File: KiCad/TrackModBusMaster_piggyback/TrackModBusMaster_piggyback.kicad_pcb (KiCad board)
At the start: 2 copper layers, 40 x 77 mm, 66 parts, among them J1 Conn_02x08_Top_Bottom, J2 Conn_02x05_Odd_Even, J3 Conn_02x08_Top_Bottom, J4 Conn_01x08, J5 Conn_01x08, Q1 NTR5103NT1G, U1 ST485EBDR, U2 ST485EBDR, U3 ST485EBDR, U4 ST485EBDR, U5 ST485EBDR, U6 PIC18F25K40

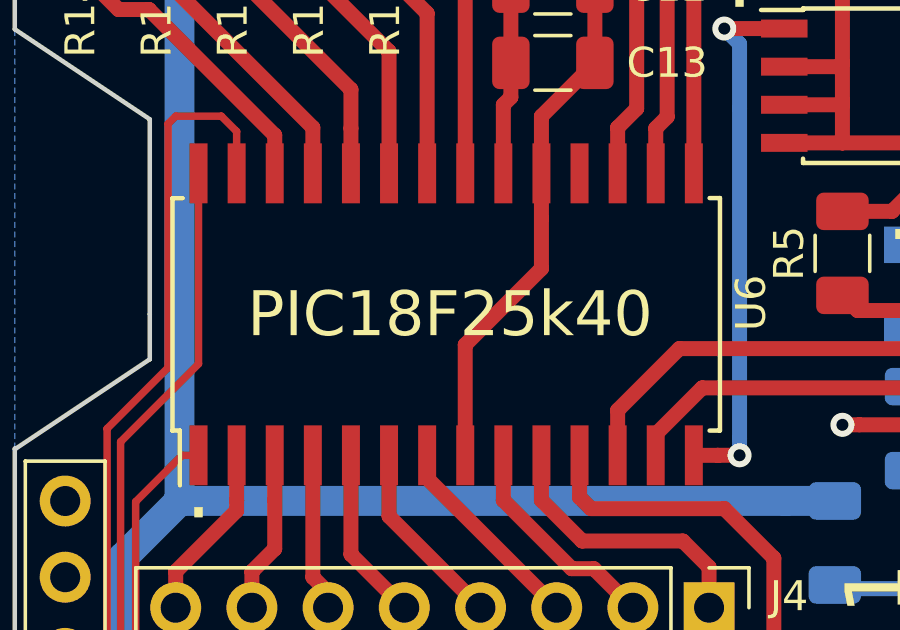
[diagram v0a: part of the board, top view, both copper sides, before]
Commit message: Updated all schematics and layouts. Updated all component lists and csv files. Created ShopCartAll.csv from farnell big order for these 4 boards. Created new gerber files in the board-named directories to be send to PCB farmer.
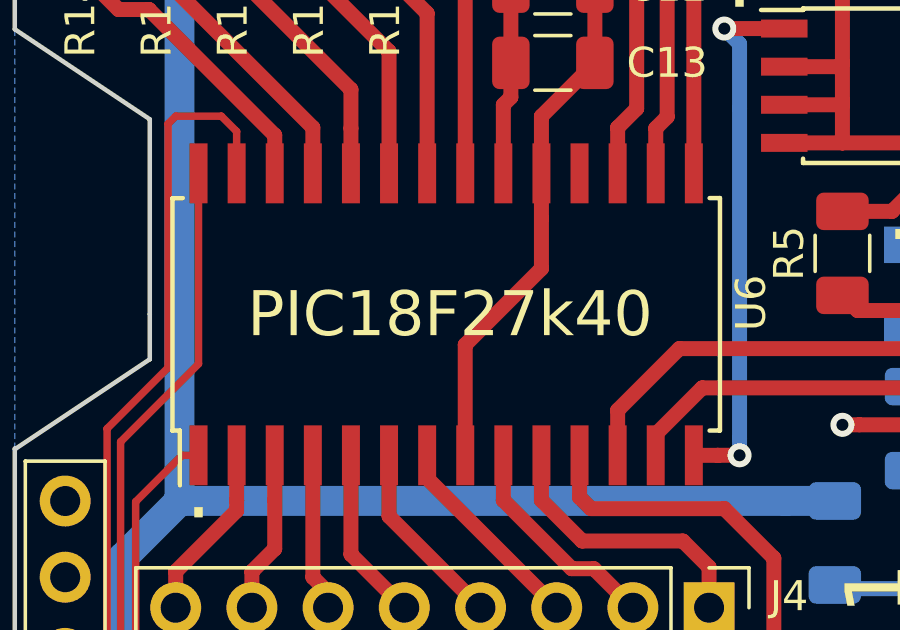
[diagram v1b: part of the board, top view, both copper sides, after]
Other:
- board text added: "PIC18F27k40"
- board text removed: "PIC18F25k40"
